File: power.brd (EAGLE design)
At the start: 186 x 186 mm, 114 parts, among them Q1 IXTK180N15P, Q2 IXTK180N15P, Q3 2N7002, Q4 SPD15P10PL, Q5 2N7002, U1 LT1630, U10 LM2936, U11 LM317, U2 LT1630, U3 DCDC 15V, U4 DAC80501, U5 DAC80501, U6 ADS1120, U7 LM2662, U8 LM7805, U9 TPS3700

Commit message: Progress on PCBs
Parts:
- added CN1: 0530471210, CONNECTORs:MOLEX_530471210
- added D8: 12V BI TVS, DIODES:DO214AC
- added MECH10, MECH11, MECH12, MECH13: 6mm x 3mm, MISC:MOUNTHOLE_6X3
- added TP1, TP2, TP3, TP4: TEST_POINT_SQUARE, MISC:OSPREY_HSS_PAD
- C27, C29, C34, C40, C44, C46, C7: value 100nF 16V -> 100nF 100V
- moved C3 328.4 mm to (2.38, -18.1), turned to 180 degrees
- moved C47 324.3 mm to (29.8, 21.2), turned to 270 degrees
- moved U11 319.4 mm to (29.8, 17.8), turned to 180 degrees
- moved C46 319.2 mm to (27.2, 21.2), turned to 270 degrees
- moved R27 315.6 mm to (31.8, 21.8)
- moved R26 313.4 mm to (31.8, 20.5), turned to 180 degrees
- moved C12 312.4 mm to (14.9, -8.12), turned to 180 degrees
- moved C17 311.6 mm to (-6.12, -9.00)
- moved FB1 308.9 mm to (3.00, 16.5), turned to 270 degrees
- moved C13 308.1 mm to (8.62, -4.38), turned to 180 degrees
- moved C10 303.4 mm to (8.62, -5.62), turned to 180 degrees
- moved C14 302.5 mm to (-6.12, -7.75)
- moved C16 301.7 mm to (-12.4, -5.25)
- moved C15 299.9 mm to (-12.4, -6.50)
- moved U8 297.4 mm to (14.8, 17.8), turned to 180 degrees
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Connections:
- net 3V3D: now also CN1.3, CN1.4
- net ADC_!DRDY: now also CN1.7
- net ADC_SPI_!CS: now also CN1.8
- net ADC_SPI_MISO: now also CN1.6
- net ADC_SPI_MOSI: now also CN1.5
- net ADC_SPI_SCLK: now also CN1.9
- net AGND: no longer C44.1, C45.1, U10.2, U10.3, U10.6, U10.7
- net DAC_I2C_SCL: now also CN1.1
- net DAC_I2C_SDA: now also CN1.2
- net DGND: now also CN1.10, CN1.11, CN1.12, U6.3
- net N$12: now also RL1.21; no longer RL1.11
- net N$14: now also RL1.11; no longer RL1.21
- net N$26: now also TP4.1
- net N$27: now also TP3.1
- net PGND: now also C44.1, C45.1, U10.2, U10.3, U10.6, U10.7
- net VOUT+: now also D8.K, RL1.24, TP1.1; no longer RL1.14
- net VOUT-: now also D8.A, RL1.14, TP2.1; no longer RL1.24
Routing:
- net GND: track 0.00 -> 354.4 mm, vias 0 -> 1
- net 15V: track 0.00 -> 347.6 mm
- net +15V: track 0.00 -> 216.4 mm, vias 0 -> 2
- net 3V3A: track 0.00 -> 120.4 mm, vias 0 -> 6
- net -5V: track 0.00 -> 77.3 mm
- net DAC_I2C_SDA: track 0.00 -> 62.5 mm
- net DAC_I2C_SCL: track 0.00 -> 61.5 mm, vias 0 -> 4
- net AGND: track 9.12 -> 68.2 mm, vias 267 -> 256
- net N$27: track 0.00 -> 55.9 mm
- net N$26: track 0.00 -> 52.0 mm
- net VIN: track 0.00 -> 49.8 mm
- net N$1: track 2.02 -> 45.9 mm, vias 2 -> 6
- net N$17: track 0.00 -> 39.2 mm, vias 0 -> 2
- net VOUT-: track 0.00 -> 35.3 mm
- net 3V3D: track 0.00 -> 24.9 mm
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- added copper zone on layer 16, net DGND
- added copper zone on layer 16, net PGND
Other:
- outline, holes or cut-outs redrawn

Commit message: Progress
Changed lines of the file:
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@@
 <setting verticaltext="up"/>
 </settings>
-<grid distance="0.125" unitdist="mm" unit="mm" style="lines" multiple="1" display="yes" altdistance="0.125" altunitdist="mm" altunit="mm"/>
+<grid distance="0.25" unitdist="mm" unit="mm" style="lines" multiple="1" display="yes" altdistance="0.125" altunitdist="mm" altunit="mm"/>
 <layers>
 <layer number="1" name="Top" color="4" fill="1" visible="yes" active="yes"/>
@@
 </layers>
 <board>
-<fusionsync huburn="a.cGVyc29uYWw6dWUyYjllNWFm" projecturn="a.cGVyc29uYWw6dWUyYjllNWFmIzIwMjAwODI1MzI2NDUzNDMx" f3durn="urn:adsk.wipprod:dm.lineage:_9x5qJVdRZCpXJjkiumNtQ" pcbguid="" lastpulledtime="" lastsyncedchangeguid="" latestrevisionid="c1cccf55-950a-498d-967b-997c356184d0" lastsyncedrevisionid="c1cccf55-950a-498d-967b-997c356184d0" lastboardhashguid="e3df3ca5-467c-2d86-2c77-ccd8f0aceb51" lastpushedtime="2020-10-02T12:40:03Z" linktopcb3d="true"/>
+<fusionsync huburn="a.cGVyc29uYWw6dWUyYjllNWFm" projecturn="a.cGVyc29uYWw6dWUyYjllNWFmIzIwMjAwODI1MzI2NDUzNDMx" f3durn="urn:adsk.wipprod:dm.lineage:_9x5qJVdRZCpXJjkiumNtQ" pcbguid="" lastpulledtime="" lastsyncedchangeguid="" latestrevisionid="8929aa9b-c4c7-4691-84ea-9a7c1afaa12d" lastsyncedrevisionid="8929aa9b-c4c7-4691-84ea-9a7c1afaa12d" lastboardhashguid="4508e98b-46b8-0a5e-579b-2bf2d418d48e" lastpushedtime="2020-10-04T12:50:42Z" linktopcb3d="true"/>
 <plain>
 <wire x1="90" y1="-93" x2="93" y2="-90" width="0" layer="20" curve="90" locked="yes"/>
@@
 <wire x1="43" y1="-65" x2="78.5" y2="-65" width="0.15" layer="21"/>
 <wire x1="78.5" y1="-65" x2="78.5" y2="-5" width="0.15" layer="21"/>
-<rectangle x1="-78.5" y1="-65" x2="-43" y2="-5" layer="21"/>
-<rectangle x1="43" y1="-65" x2="78.5" y2="-5" layer="21"/>
 <wire x1="-22.5" y1="-68" x2="-19.5" y2="-65" width="0" layer="20" curve="-90" locked="yes"/>
 <wire x1="-19.5" y1="-65" x2="-10.5" y2="-65" width="0" layer="20" locked="yes"/>

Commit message: Progress
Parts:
- added MECH14, MECH15: 6mm x 3mm, MISC:MOUNTHOLE_6X3
- moved L3 11.3 mm to (31.0, -11.2)
- moved C9 11.3 mm to (36.5, -23.2), turned to 0 degrees
- moved C37 7.69 mm to (-0.88, 23.0)
- moved C38 7.69 mm to (-0.88, 13.5)
- moved C39 7.69 mm to (2.50, 15.9)
- moved C42 7.69 mm to (-0.88, 8.75)
- moved FB1 7.69 mm to (-2.50, 11.1)
- moved U7 7.69 mm to (-0.62, 18.2)
- moved C40 7.07 mm to (12.2, 26.2)
- moved C41 7.07 mm to (7.25, 26.2)
- moved C46 7.07 mm to (22.2, 26.2)
- moved C47 7.07 mm to (24.8, 26.2)
- moved R26 7.07 mm to (26.8, 25.5)
- moved R27 7.07 mm to (26.8, 26.8)
- moved U11 7.07 mm to (24.8, 22.8)
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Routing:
- net N$33: track 8.57 -> 16.7 mm
- net -5V: track 77.3 -> 74.7 mm
- net DAC_I2C_SDA: track 62.5 -> 60.3 mm
- net DAC_I2C_SCL: track 61.5 -> 59.3 mm
- net 3V3A: track 120.4 -> 119.6 mm, vias 6 -> 4
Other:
- outline, holes or cut-outs redrawn

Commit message: Control nearly done
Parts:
- removed CN1: 0530471210, CONNECTORs:MOLEX_530471210
- added CN2: 2X10 HEADER, CONNECTORs:2X10PIN_HEADER
- moved R18 30.5 mm to (-60.5, 3.88)
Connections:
- removed net N$36: Q4.2, U3.2
- new net VOUT: CN2.13, CN2.14, CN2.7, CN2.8, Q4.2, U3.2
- net 3V3D: now also CN2.19, CN2.2; no longer CN1.3, CN1.4
- net ADC_!DRDY: now also CN2.5; no longer CN1.7
- net ADC_SPI_!CS: now also CN2.15; no longer CN1.8
- net ADC_SPI_MISO: now also CN2.4; no longer CN1.6
- net ADC_SPI_MOSI: now also CN2.3; no longer CN1.5
- net ADC_SPI_SCLK: now also CN2.6; no longer CN1.9
- net DAC_I2C_SCL: now also CN2.17; no longer CN1.1
- net DAC_I2C_SDA: now also CN2.18; no longer CN1.2
- net DGND: now also CN2.1, CN2.16, CN2.20; no longer CN1.10, CN1.11, CN1.12
- net PGND: now also CN2.10, CN2.11, CN2.12, CN2.9
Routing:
- net VOUT: track 0.00 -> 86.8 mm
- net PGND: track 14.2 -> 60.7 mm, vias 12 -> 17
- net DAC_I2C_SCL: track 59.3 -> 82.0 mm
- net DAC_I2C_SDA: track 60.3 -> 79.3 mm
- net 3V3D: track 24.9 -> 41.2 mm
- net N$36: track 14.6 -> 0.00 mm
- net ADC_SPI_!CS: track 20.7 -> 33.9 mm
- net ADC_!DRDY: track 19.6 -> 30.1 mm
- net ADC_SPI_SCLK: track 17.5 -> 26.1 mm
- net ADC_SPI_MISO: track 19.2 -> 27.2 mm
- net ADC_SPI_MOSI: track 18.9 -> 24.4 mm

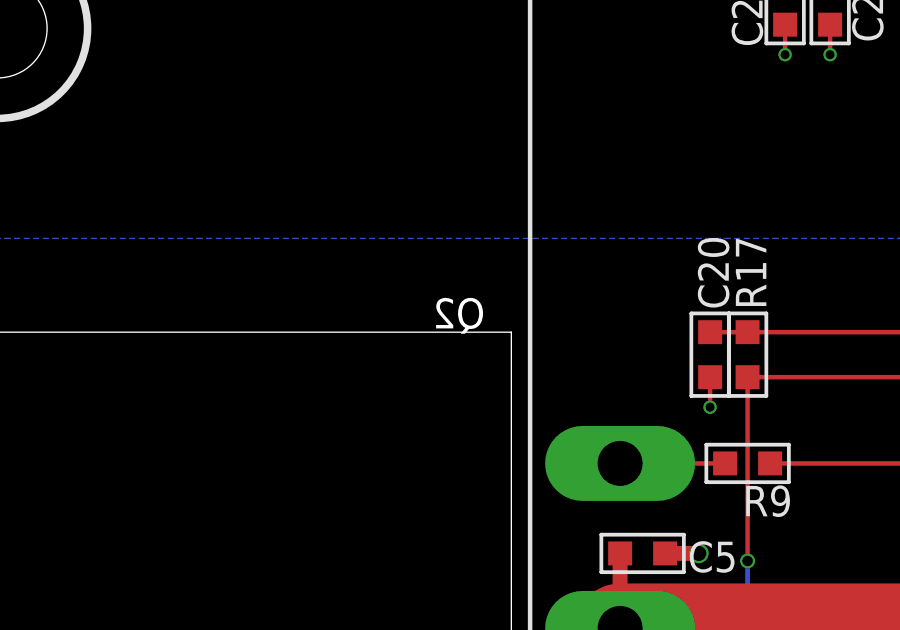
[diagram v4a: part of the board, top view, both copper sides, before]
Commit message: Female header added to the power PCB
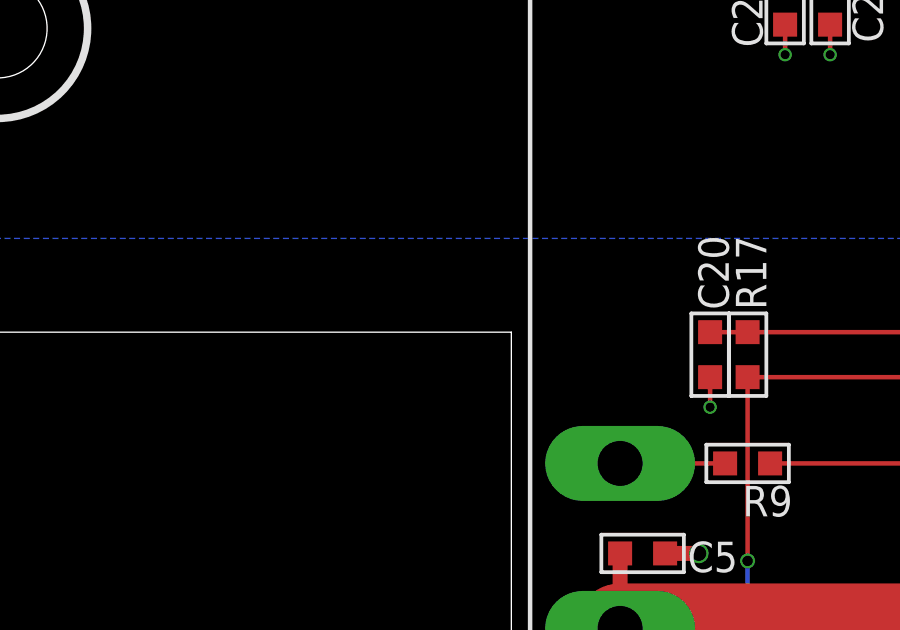
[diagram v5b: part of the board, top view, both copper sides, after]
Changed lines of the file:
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@@
 <setting verticaltext="up"/>
 </settings>
-<grid distance="0.125" unitdist="mm" unit="mm" style="lines" multiple="1" display="yes" altdistance="0.125" altunitdist="mm" altunit="mm"/>
+<grid distance="0.25" unitdist="mm" unit="mm" style="lines" multiple="1" display="yes" altdistance="0.125" altunitdist="mm" altunit="mm"/>
 <layers>
 <layer number="1" name="Top" color="4" fill="1" visible="yes" active="yes"/>
@@
 <element name="Q2" library="TRANSISTORs" package="TO264F" value="IXTK180N15P" x="-40" y="-35" smashed="yes" rot="MR270">
 <attribute name="FARNELL" value="1427360" x="-36.19" y="-79.45" size="1.778" layer="28" rot="MR270" display="off"/>
-<attribute name="NAME" x="-44.5" y="-25" size="1" layer="20" rot="MR0"/>
+<attribute name="NAME" x="-44.5" y="-25" size="1" layer="22" rot="MR0"/>
 <attribute name="PRICE_PER" value="9.57" x="-36.19" y="-79.45" size="1.778" layer="28" rot="MR270" display="off"/>
 </element>
@@
 <element name="MECH15" library="MISC" package="MOUNTHOLE_6X3" value="6mm x 3mm" x="24.75" y="6.75" locked="yes" smashed="yes"/>
 <element name="CN2" library="CONNECTORs" package="2X10PIN_HEADER" value="2X10 HEADER" x="-60" y="0" smashed="yes" rot="MR90">
-<attribute name="DIGIKEY" value="2057-PH2-20-UA-ND" x="-60" y="0" size="1.778" layer="28" rot="MR90" display="off"/>
-<attribute name="HEIGHT" value="10" x="-60" y="0" size="1.778" layer="28" rot="MR90" display="off"/>
+<attribute name="DIGIKEY" value="2057-RS2-20-G-ND" x="-60" y="0" size="1.778" layer="28" rot="MR90" display="off"/>
+<attribute name="HEIGHT" value="8.5" x="-60" y="0" size="1.778" layer="28" rot="MR90" display="off"/>
 <attribute name="NAME" x="-46.21" y="-2.52" size="1" layer="26" rot="MR90"/>
-<attribute name="PRICE_PER" value="0.2" x="-60" y="0" size="1.778" layer="28" rot="MR90" display="off"/>
+<attribute name="PRICE_PER" value="0.85" x="-60" y="0" size="1.778" layer="28" rot="MR90" display="off"/>
 </element>
 </elements>
